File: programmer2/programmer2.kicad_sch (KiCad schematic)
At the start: 61 parts, among them J1 USB_C_Receptacle_USB2.0_14P, U1 FT2232HL, U3 93CxxA, U4 MIC5504-1.8YM5, U8 AMS1117-3.3, Y1 12MHz

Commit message: Finished programmer 2.
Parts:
- added TP7, TP8: TestPoint, TestPoint:TestPoint_THTPad_1.0x1.0mm_Drill0.5mm, symbol Connector:TestPoint
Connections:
- net FT_JTAG_SEL_N: now also U_EPLD1.25 (I/O); no longer U_EPLD1.20 (I/O)
- net FT_JTAG_TCK: now also U_EPLD1.30 (I/O); no longer U_EPLD1.29 (I/O)
- net FT_JTAG_TDI: now also U_EPLD1.28 (I/O); no longer U_EPLD1.24 (I/O)
- net FT_JTAG_TDO: now also U_EPLD1.27 (I/O); no longer U_EPLD1.22 (I/O)
- net FT_JTAG_TMS: now also U_EPLD1.26 (I/O); no longer U_EPLD1.21 (I/O)
- net FT_RECONFIG_N: now also U_EPLD1.24 (I/O); no longer U_EPLD1.19 (I/O)
- net IO4A: now also U_EPLD1.44 (I/O); no longer U_EPLD1.38 (I/O)
- net IO4B: now also U_EPLD1.43 (I/O); no longer U_EPLD1.37 (I/O)
- net JTAG_LED: now also U_EPLD1.29 (I/O); no longer U_EPLD1.30 (I/O)
- net SER_RXD: now also U_EPLD1.42 (I/O); no longer U_EPLD1.35 (I/O)
- net SER_TXD: now also U_EPLD1.40 (I/O); no longer U_EPLD1.34 (I/O)
- net at TP2.1: now also U_EPLD1.35 (I/O); no longer U1.33 (ACBUS6)
- net at TP3.1: now also U_EPLD1.36 (I/O); no longer U1.34 (ACBUS7)
- net FT_ACBUS3: now reaches U1.29 (ACBUS3)
- net FT_ACBUS3: now also U_EPLD1.22 (I/O)
- net FT_ACBUS4: now reaches U1.30 (ACBUS4)
- net FT_ACBUS4: now also U_EPLD1.21 (I/O)
- net at TP1.1: now also U_EPLD1.34 (I/O); no longer U1.32 (ACBUS5)
- net FT_ACBUS7: now reaches U_EPLD1.18 (I/O)
- net FT_ACBUS7: now also U1.34 (ACBUS7)
- new net: TP7.1, U_EPLD1.37 (I/O)
- new net: TP8.1, U_EPLD1.38 (I/O)
- new net FT_ACBUS5: U1.32 (ACBUS5), U_EPLD1.20 (I/O)
- new net FT_ACBUS6: U1.33 (ACBUS6), U_EPLD1.19 (I/O)
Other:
- moved on the sheet: TP1, TP2, TP3

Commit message: Beautified schematic and PCB for programmer 2.
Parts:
- D4, D5: footprint LED_SMD:LED_0603_1608Metric_Pad1.05x0.95mm_HandSolder -> unic:LED_0603_1608Metric_Pad1.05x0.95mm_HandSolder
- H1, H2, H3, H4: footprint MountingHole:MountingHole_3.2mm_M3_DIN965_Pad -> unic:MountingHole_3.2mm_M3_DIN965_Pad
- TP1, TP2, TP3, TP4, TP5, TP6, TP7, TP8: footprint TestPoint:TestPoint_THTPad_1.0x1.0mm_Drill0.5mm -> unic:TestPoint_THTPad_1.0x1.0mm_Drill0.5mm
- renumbered J_EXT1 to J2, J_EXT2 to J3, U_EPLD1 to U2
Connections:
- net GND: now also D4.1 (K)
- net JTAG_LED: now also R10.1; no longer R10.2
- net VCC: no longer D4.1 (K)
- net VIO: now also D5.2 (A); no longer D5.1 (K)
- net at R11.1: now also D5.1 (K); no longer D5.2 (A)
- net VPHY: now reaches C2.1, R2.2, U1.4 (VPHY)
- net VPLL: now reaches C1.1, R1.2, U1.9 (VPLL)
- net at D4.2 (A): now also R10.2; no longer R10.1
- net VCORE renamed V_FCORE
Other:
- title: UNIC 40 -> UNIC Programmer 2
- moved on the sheet: C1, C10, C11, C12, C13, C14, C15, C16, C17, C19, C2, C23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

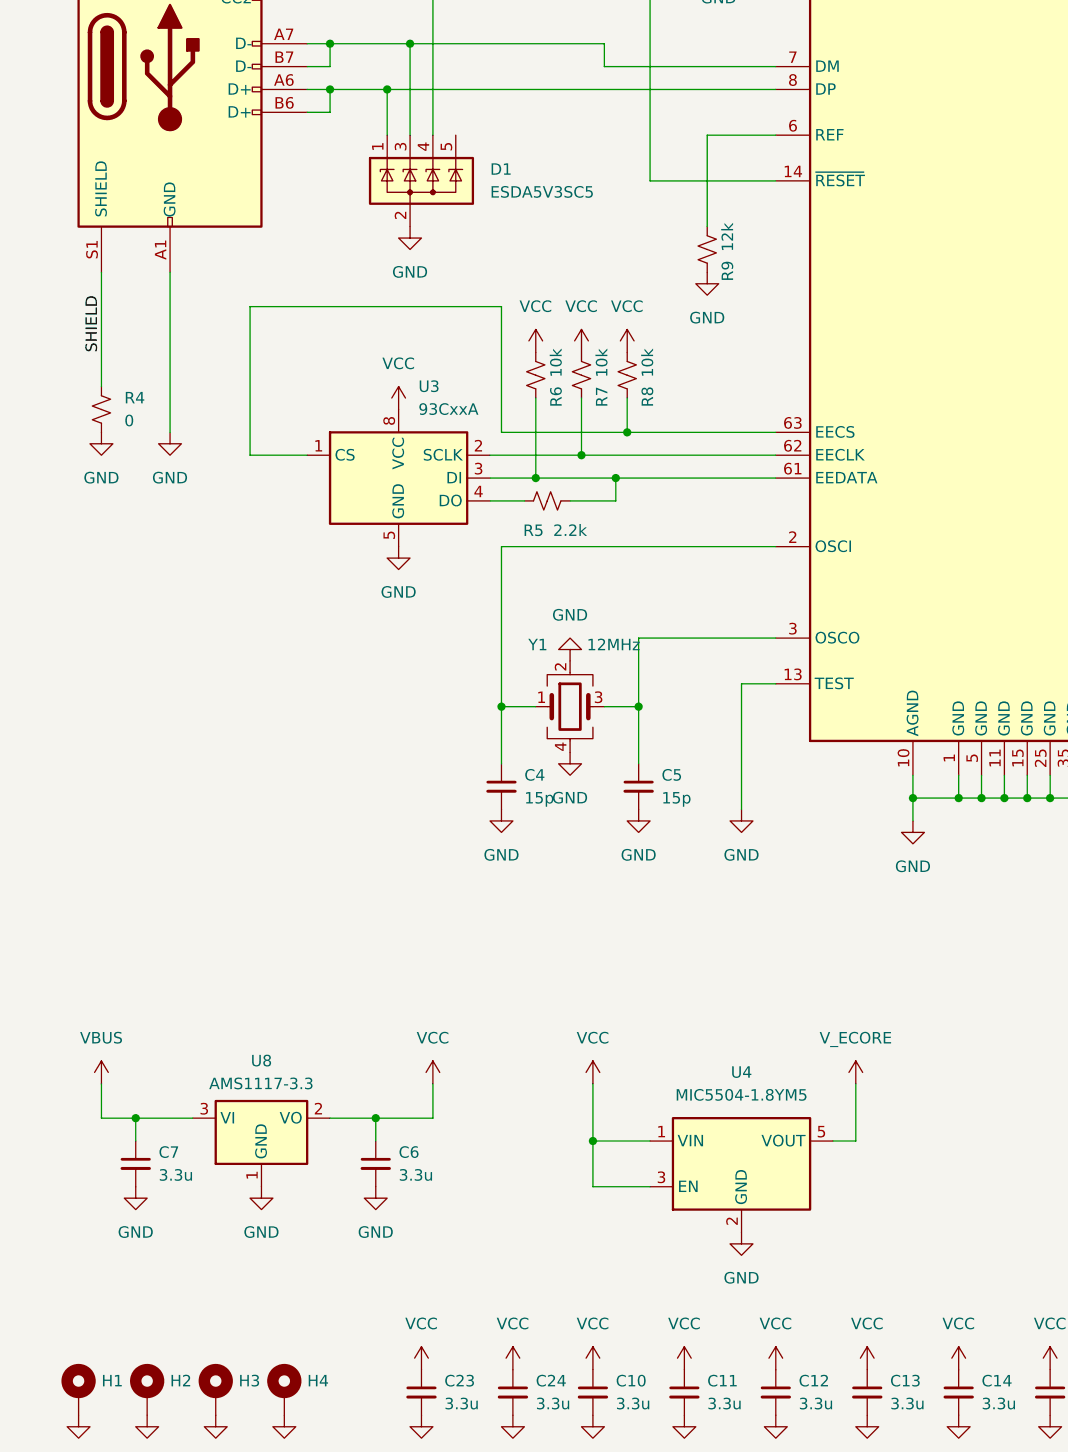
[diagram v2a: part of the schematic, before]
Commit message: Updated programmer schematic and PCBs.
All known changes are incorporated.

p.s.: I decided to stick with this rather sketchy LDO.
The reason for this is that it's heatsink tab is connected
to VCC, which happens to be the fill on the top layer
so a GND-connected alternative would be less well cooled.
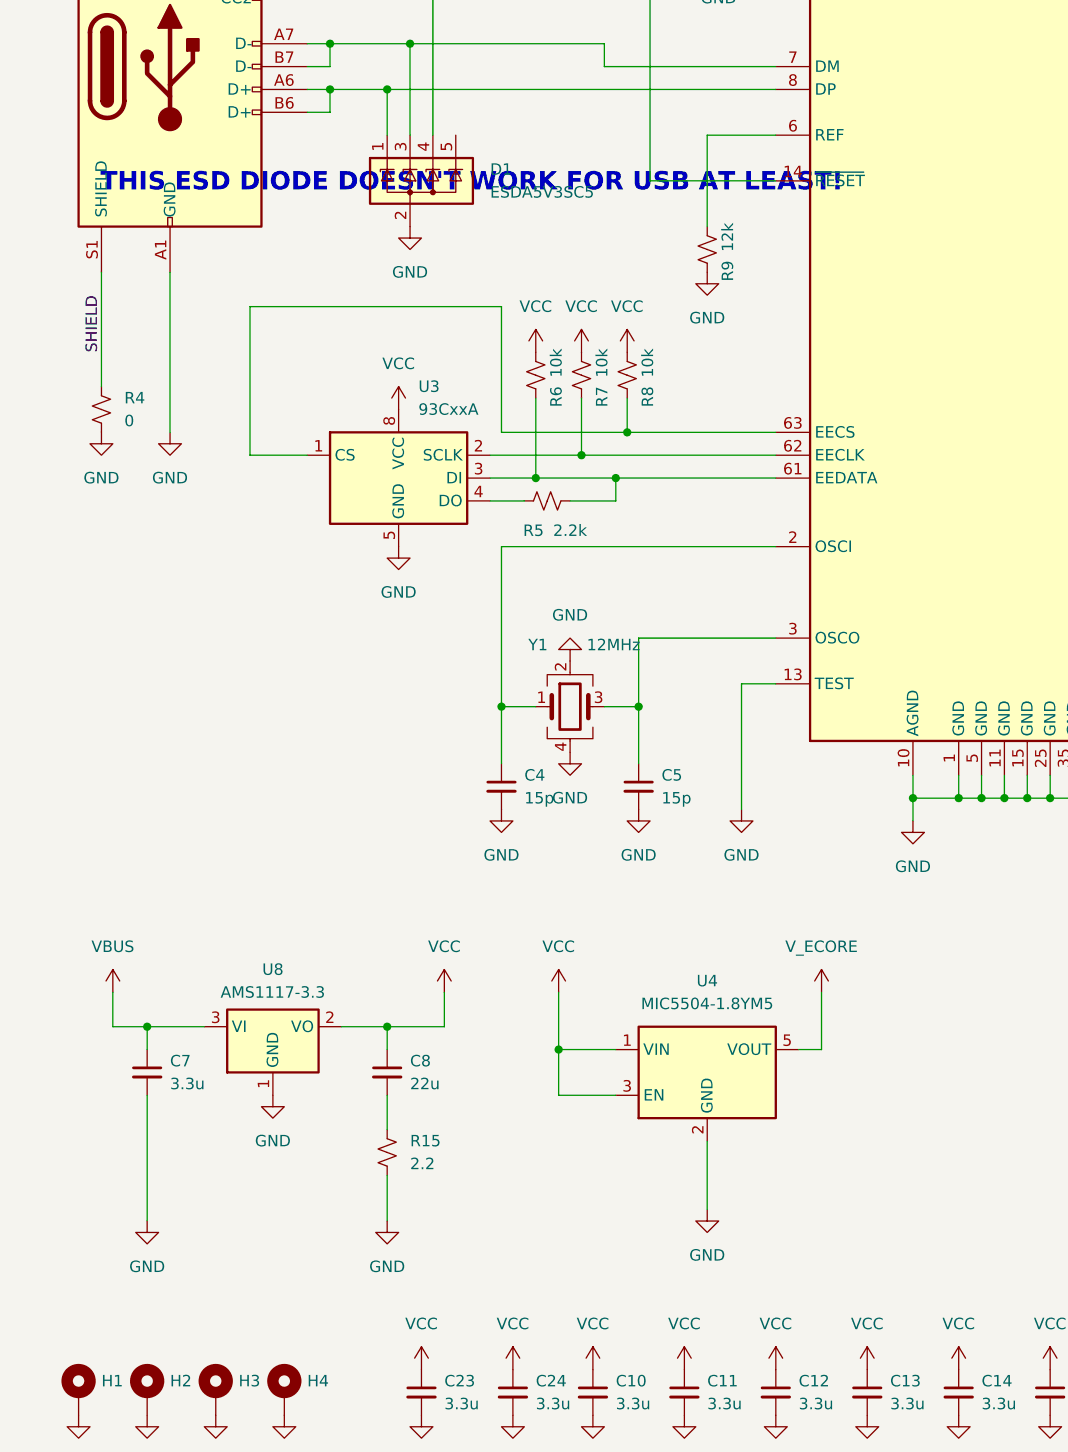
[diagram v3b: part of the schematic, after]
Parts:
- removed C6: 3.3u, Capacitor_SMD:C_0603_1608Metric_Pad1.08x0.95mm_HandSolder, symbol Device:C_Small
- added C8: 22u, Capacitor_SMD:C_0805_2012Metric_Pad1.18x1.45mm_HandSolder, symbol Device:C_Small
- added R15: 2.2, Resistor_SMD:R_0603_1608Metric_Pad0.98x0.95mm_HandSolder, symbol Device:R_Small_US
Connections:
- net GND: now also R15.2
- net VCC: now also C8.1
- new net: C8.2, R15.1
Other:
- note added: "THIS ESD DIODE DOESN'T WORK FOR USB AT LEAST!"
- moved on the sheet: C7, U4, U8
